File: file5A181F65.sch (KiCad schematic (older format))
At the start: 20 parts, among them Q1 BF824, Q2 MMBT3904, Q3 BF820, Q4 BF824, Q5 MMBT3904

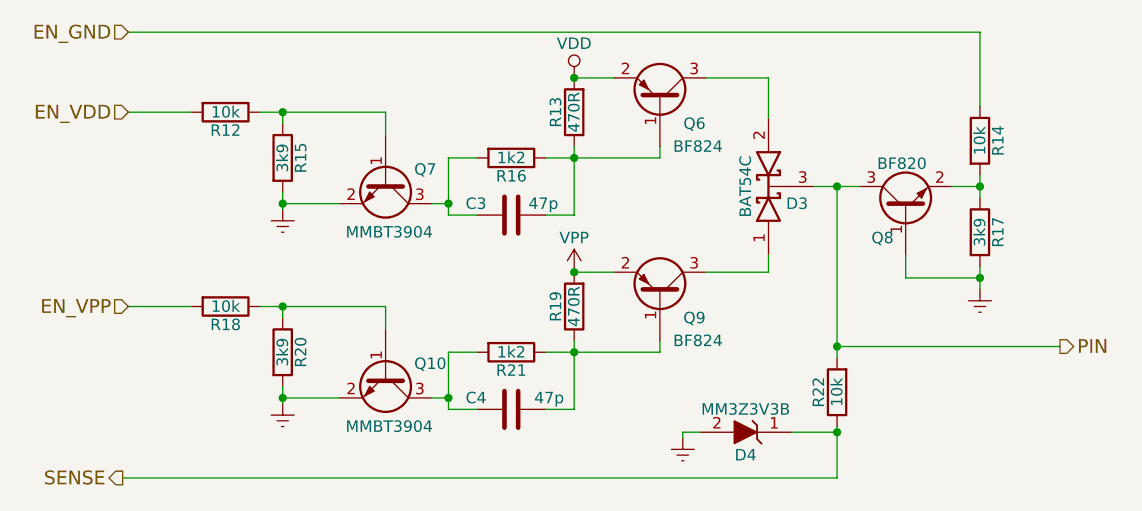
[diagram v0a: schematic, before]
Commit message: Adds to schematic
Duplicates pin drivers x40, adds connectors.
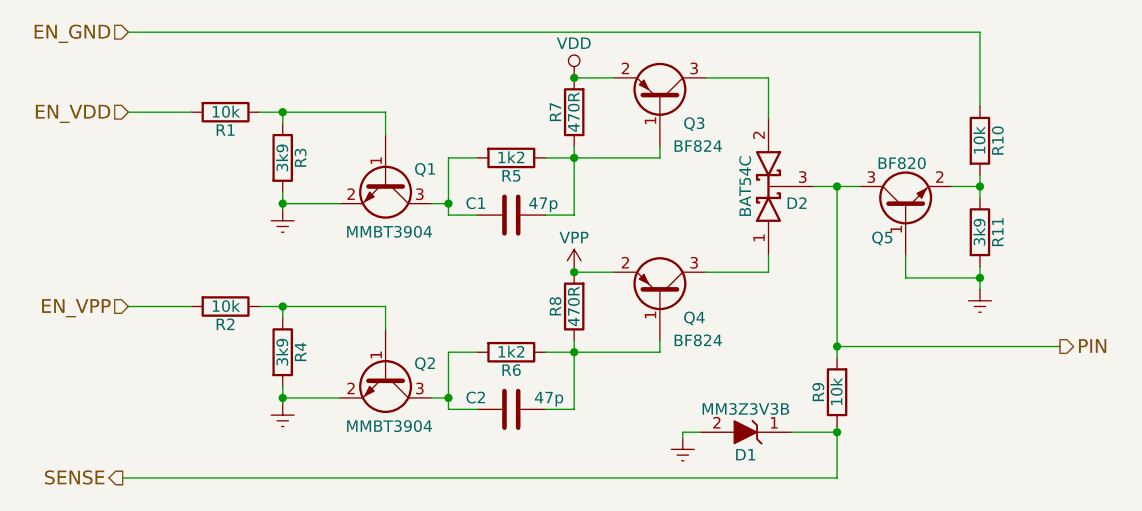
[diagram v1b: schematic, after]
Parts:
- C1, C2: footprint (none) -> Capacitors_SMD:C_0603_HandSoldering; MFG (none) -> -; MFG P/N (none) -> -
- D1: renamed from D2; footprint (none) -> Diodes_SMD:D_SOD-323_HandSoldering; MFG (none) -> -; MFG P/N (none) -> -
- D2: renamed from D1; footprint (none) -> TO_SOT_Packages_SMD:SOT-23_Handsoldering; MFG (none) -> -; MFG P/N (none) -> -
- Q1: renamed from Q2; footprint SOT-23 -> TO_SOT_Packages_SMD:SOT-23_Handsoldering; MFG (none) -> -; MFG P/N (none) -> -
- Q2: renamed from Q5; footprint SOT-23 -> TO_SOT_Packages_SMD:SOT-23_Handsoldering; MFG (none) -> -; MFG P/N (none) -> -
- Q3: renamed from Q1; footprint (none) -> TO_SOT_Packages_SMD:SOT-23_Handsoldering; MFG (none) -> -; MFG P/N (none) -> -
- Q4: footprint (none) -> TO_SOT_Packages_SMD:SOT-23_Handsoldering; MFG (none) -> -; MFG P/N (none) -> -
- Q5: renamed from Q3; footprint (none) -> TO_SOT_Packages_SMD:SOT-23_Handsoldering; MFG (none) -> -; MFG P/N (none) -> -
- R1, R5, R8: footprint (none) -> Resistors_SMD:R_0603_HandSoldering; MFG (none) -> -; MFG P/N (none) -> -
- R10: renamed from R3; footprint (none) -> Resistors_SMD:R_0603_HandSoldering; MFG (none) -> -; MFG P/N (none) -> -
- R11: renamed from R6; footprint (none) -> Resistors_SMD:R_0603_HandSoldering; MFG (none) -> -; MFG P/N (none) -> -
- R2: renamed from R7; footprint (none) -> Resistors_SMD:R_0603_HandSoldering; MFG (none) -> -; MFG P/N (none) -> -
- R3: renamed from R4; footprint (none) -> Resistors_SMD:R_0603_HandSoldering; MFG (none) -> -; MFG P/N (none) -> -
- R4: renamed from R9; footprint (none) -> Resistors_SMD:R_0603_HandSoldering; MFG (none) -> -; MFG P/N (none) -> -
- R6: renamed from R10; footprint (none) -> Resistors_SMD:R_0603_HandSoldering; MFG (none) -> -; MFG P/N (none) -> -
- R7: renamed from R2; footprint (none) -> Resistors_SMD:R_0603_HandSoldering; MFG (none) -> -; MFG P/N (none) -> -
- R9: renamed from R11; footprint (none) -> Resistors_SMD:R_0603_HandSoldering; MFG (none) -> -; MFG P/N (none) -> -
